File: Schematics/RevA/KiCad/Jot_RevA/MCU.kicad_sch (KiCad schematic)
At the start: 0 parts

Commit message: KiCad MCU: place U1 MDBT50Q-1MV2 module
Co-Authored-By: Claude Opus 5.5 <noreply@anthropic.com>
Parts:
- added U1: MDBT50Q-1MV2, RF_Module:Raytac_MDBT50Q, symbol RF_Module:MDBT50Q-1MV2
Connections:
- new net: U1.1 (GND), U1.15 (GND), U1.2 (GND), U1.33 (GND), U1.55 (GND)
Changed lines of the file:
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@@
 	(generator_version "10.0")
 	(paper "A4")
+	(symbol
+		(lib_id "RF_Module:MDBT50Q-1MV2")
+		(at 142.24 91.44 0)
+		(unit 1)
+		(body_style 1)
+		(exclude_from_sim no)
+		(in_bom yes)
+		(on_board yes)
+		(in_pos_files yes)
+		(dnp no)
+		(fields_autoplaced yes)
+		(property "Reference" "U1"
+			(at 144.3833 137.16 0)
+			(show_name no)
+			(do_not_autoplace no)
+			(effects
+				(font
+					(size 1.27 1.27)
+				)
+				(justify left)
+			)
+		)
+		(property "Value" "MDBT50Q-1MV2"
+			(at 144.3833 139.7 0)
+			(show_name no)
+			(do_not_autoplace no)
+			(effects
+				(font
+					(size 1.27 1.27)
+				)
+				(justify left)
+			)
+		)
+		(property "Footprint" "RF_Module:Raytac_MDBT50Q"
+			(at 142.24 96.52 0)
+			(hide yes)
+			(show_name no)
+			(do_not_autoplace no)
+			(effects
+				(font
+					(size 1.27 1.27)
+				)
+			)
+		)
+		(property "Datasheet" "https://www.raytac.com/download/index.php?index_id=43"
+			(at 142.24 96.52 0)
+			(hide yes)
+			(show_name no)
+			(do_not_autoplace no)
+			(effects
+				(font
+					(size 1.27 1.27)
+				)
+			)
+		)
+		(property "Description" "Multiprotocol BLE/ANT/2.4 GHz/802.15.4 Cortex-M4F SoC, nRF52840 module"
+			(at 142.24 91.44 0)
+			(hide yes)
+			(show_name no)
+			(do_not_autoplace no)
+			(effects
+				(font
+					(size 1.27 1.27)
+				)
+			)
+		)
+		(pin "46"
+		)
+		(pin "37"
+		)
+		(pin "36"
+		)
+		(pin "10"
+		)
+		(pin "11"
+		)
+		(pin "12"
+		)
+		(pin "47"
+		)
+		(pin "48"
+		)
+		(pin "56"
+		)
+		(pin "57"
+		)
+		(pin "61"
+		)
+		(pin "58"
+		)
+		(pin "59"
+		)
+		(pin "60"
+		)
+		(pin "31"
+		)
+		(pin "32"
+		)
+		(pin "28"
+		)
+		(pin "34"
+		)
+		(pin "35"
+		)
+		(pin "29"
+		)
+		(pin "30"
+		)
+		(pin "33"
+		)
+		(pin "6"
+		)
+		(pin "5"
+		)
+		(pin "8"
+		)
+		(pin "7"
+		)
+		(pin "9"
+		)
+		(pin "4"
+		)
+		(pin "3"
+		)
+		(pin "2"
+		)
+		(pin "1"
+		)
+		(pin "49"
+		)
+		(pin "17"
+		)
+		(pin "18"
+		)
+		(pin "13"
+		)
+		(pin "14"
+		)
+		(pin "15"
+		)
+		(pin "16"
+		)
+		(pin "19"
+		)
+		(pin "27"
+		)
+		(pin "20"
+		)
+		(pin "26"
+		)
+		(pin "25"
+		)
+		(pin "21"
+		)
+		(pin "22"
+		)
+		(pin "23"
+		)
+		(pin "24"
+		)
+		(pin "44"
+		)
+		(pin "45"
+		)
+		(pin "42"
+		)
+		(pin "43"
+		)
+		(pin "41"
+		)
+		(pin "40"
+		)
+		(pin "39"
+		)
+		(pin "38"
+		)
+		(pin "55"
+		)
+		(pin "54"
+		)
+		(pin "53"
+		)
+		(pin "52"
+		)
+		(pin "51"
+		)
+		(pin "50"
+		)
+		(instances
+			(project "Jot_RevA"
+				(path "/61747270-9f90-47b6-9c50-5ea1f41f259a/12d7af8c-4dae-4738-915d-dcd3faf7f757"
+					(reference "U1")
+					(unit 1)
+				)
+			)
+		)
+	)
 )

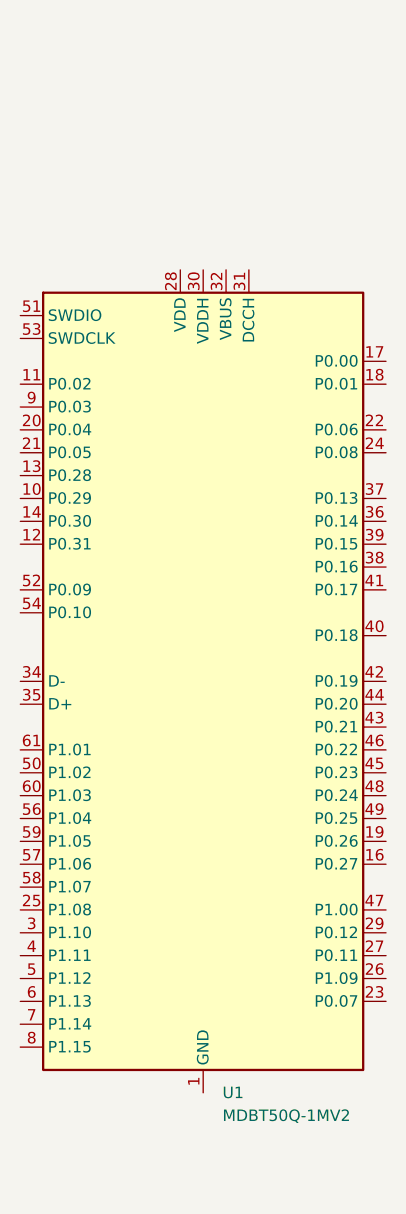
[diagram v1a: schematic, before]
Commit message: KiCad MCU: U1 VDD/VDDH on +3V3 with 10uF, grounds
Co-Authored-By: Claude Opus 5.5 <noreply@anthropic.com>
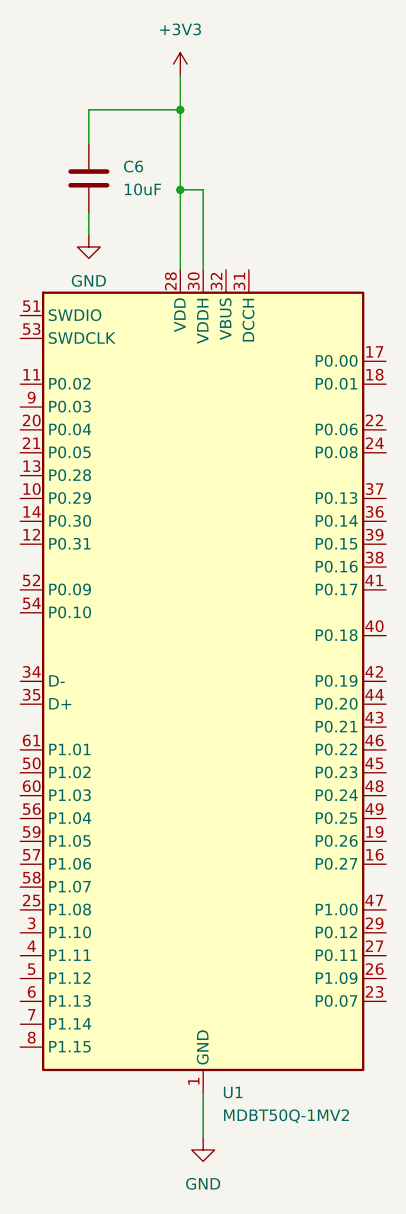
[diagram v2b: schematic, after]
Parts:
- added C6: 10uF, Package_SO:SOIC-8_3.9x4.9mm_P1.27mm, symbol Device:C
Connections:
- net GND: now reaches U1.1 (GND), U1.15 (GND), U1.2 (GND), U1.33 (GND), U1.55 (GND)
- net GND: now also C6.2
- net +3V3: now reaches U1.28 (VDD)
- net +3V3: now also U1.30 (VDDH), C6.1

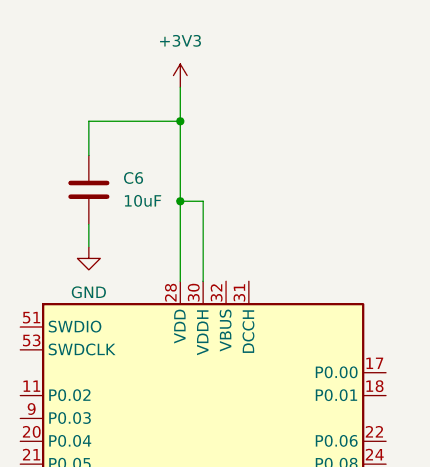
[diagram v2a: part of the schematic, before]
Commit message: KiCad MCU: VBUS via R14 2.2R with 10uF, PWR_FLAG, DCCH no-connect
Co-Authored-By: Claude Opus 5.5 <noreply@anthropic.com>
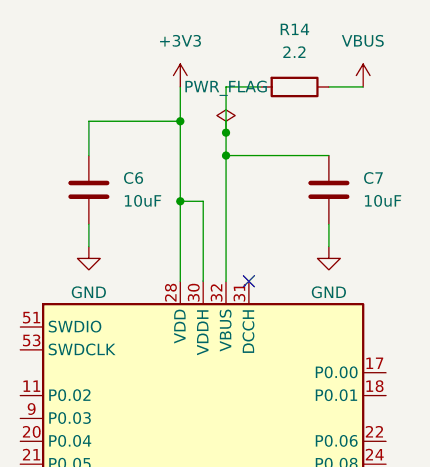
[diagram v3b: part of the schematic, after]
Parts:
- added C7: 10uF, Package_SO:SOIC-8_3.9x4.9mm_P1.27mm, symbol Device:C
- added R14: 2.2, symbol Device:R
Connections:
- net GND: now also C7.2
- net at U1.32 (VBUS): now also C7.1, R14.2
- new net VBUS: R14.1
- no-connect marks 0 -> 1

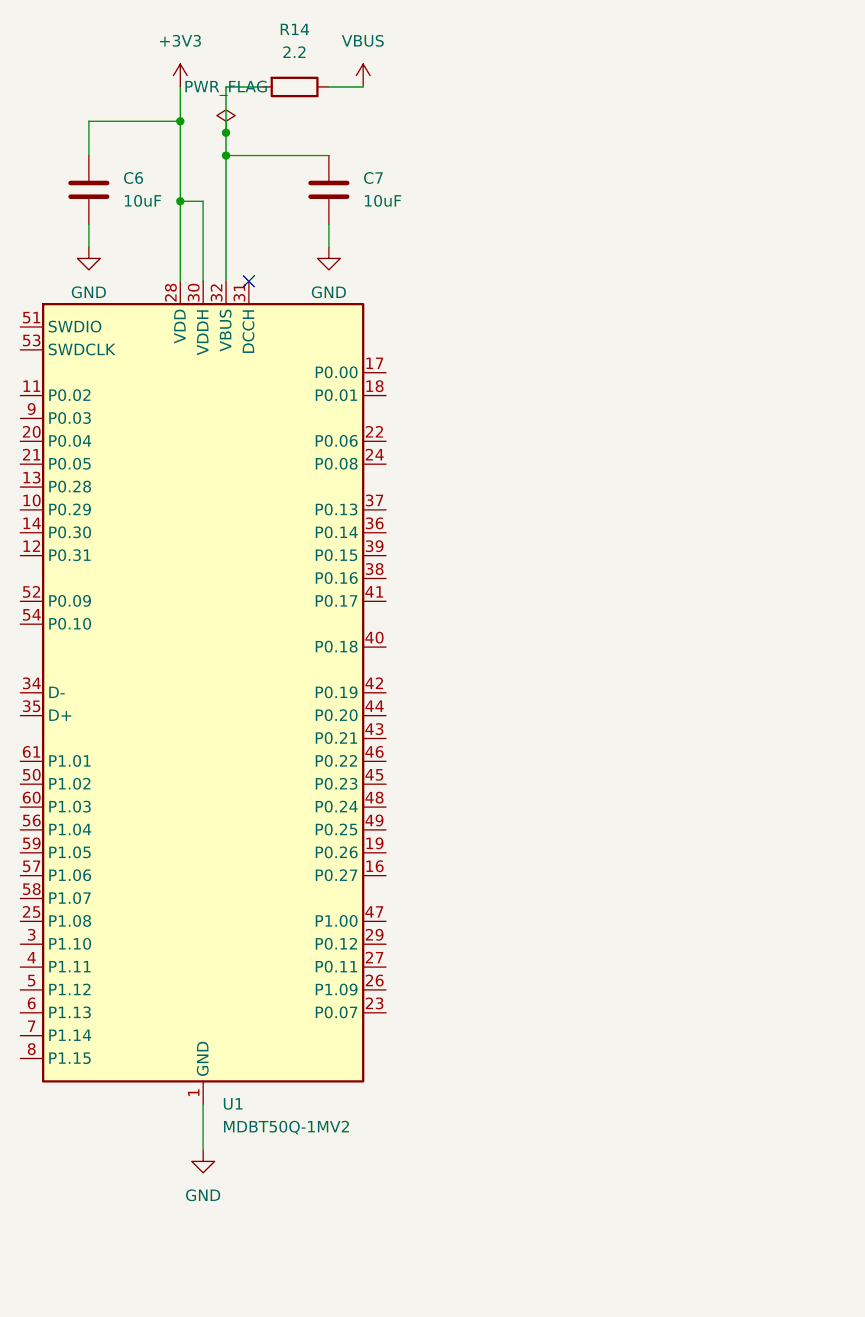
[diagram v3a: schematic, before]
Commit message: KiCad: tidy MCU power cluster and spacing; fill MCU/Power title blocks
Co-Authored-By: Claude Opus 5.5 <noreply@anthropic.com>
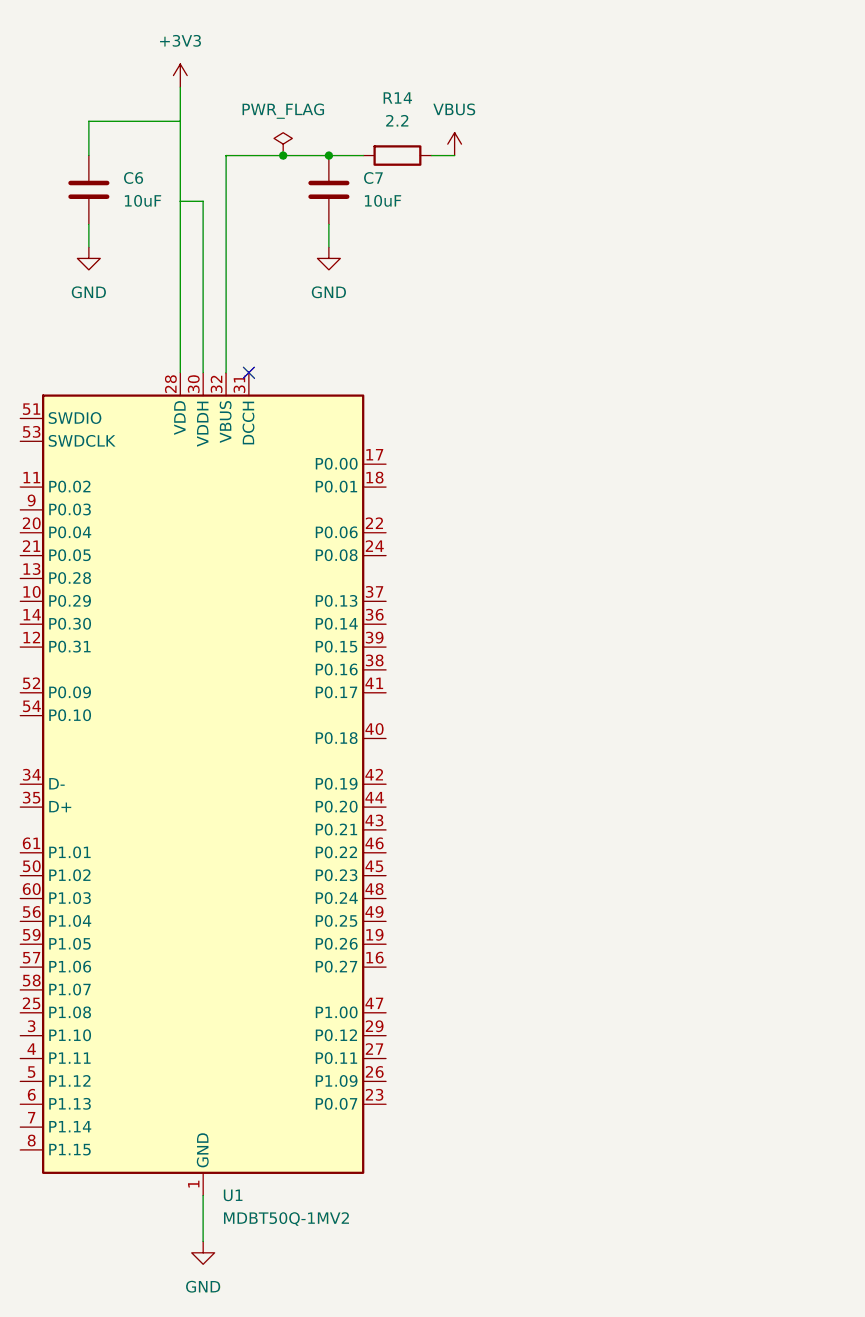
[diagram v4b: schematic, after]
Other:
- company: (none) -> James Donal Cronin
- title: (none) -> Jot Rev A: MCU
- moved on the sheet: R14, U1
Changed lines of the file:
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@@
 	(generator_version "10.0")
 	(paper "A4")
+	(title_block
+		(title "Jot Rev A: MCU")
+		(date "2026-10-02")
+		(rev "A")
+		(company "James Donal Cronin")
+		(comment 1 "JOT-HW-001: handheld push-to-talk voice capture")
+	)
+	(no_connect
+		(at 147.32 55.88)
+	)
+	(wire
+		(pts
+			(xy 144.78 31.75) (xy 151.13 31.75)
+		)
+		(stroke
+			(width 0)
+			(type default)
+		)
+	)
+	(wire
+		(pts
+			(xy 151.13 31.75) (xy 156.21 31.75)
+		)
+		(stroke
+			(width 0)
+			(type default)
+		)
+	)
+	(wire
+		(pts
+			(xy 156.21 31.75) (xy 160.02 31.75)
+		)
+		(stroke
+			(width 0)
+			(type default)
+		)
+	)
+	(wire
+		(pts
+			(xy 167.64 31.75) (xy 170.18 31.75)
+		)
+		(stroke
+			(width 0)
+			(type default)
+		)
+	)
 	(junction
-		(at 139.7 27.94)
+		(at 151.13 31.75)
 		(diameter 0)
 		(color 0 0 0 0)
 	)
 	(junction
-		(at 144.78 29.21)
+		(at 156.21 31.75)
 		(diameter 0)
 		(color 0 0 0 0)
 	)
-	(junction
-		(at 139.7 36.83)
-		(diameter 0)
-		(color 0 0 0 0)
-	)
-	(junction
-		(at 144.78 31.75)
-		(diameter 0)
-		(color 0 0 0 0)
-	)
-	(no_connect
-		(at 147.32 45.72)
-	)
 	(wire
 		(pts
@@
 	(wire
 		(pts
-			(xy 139.7 36.83) (xy 139.7 45.72)
-		)
-		(stroke
-			(width 0)
-			(type default)
-		)
-	)
-	(wire
-		(pts
-			(xy 144.78 29.21) (xy 144.78 24.13)
-		)
-		(stroke
-			(width 0)
-			(type default)
-		)
-	)
-	(wire
-		(pts
-			(xy 144.78 45.72) (xy 144.78 31.75)
-		)
-		(stroke
-			(width 0)
-			(type default)
-		)
-	)
-	(wire
-		(pts
-			(xy 142.24 45.72) (xy 142.24 36.83)
+			(xy 139.7 36.83) (xy 139.7 55.88)
+		)
+		(stroke
+			(width 0)
+			(type default)
+		)
+	)
+	(wire
+		(pts
+			(xy 144.78 55.88) (xy 144.78 31.75)
+		)
+		(stroke
+			(width 0)
+			(type default)
+		)
+	)
+	(wire
+		(pts
+			(xy 142.24 55.88) (xy 142.24 36.83)
 		)
 		(stroke
@@
 	(wire
 		(pts
-			(xy 144.78 31.75) (xy 156.21 31.75)
-		)
-		(stroke
-			(width 0)
-			(type default)
-		)
-	)
-	(wire
-		(pts
-			(xy 144.78 31.75) (xy 144.78 29.21)
-		)
-		(stroke
-			(width 0)
-			(type default)
-		)
-	)
-	(wire
-		(pts
 			(xy 139.7 27.94) (xy 139.7 36.83)
 		)
@@
 	(wire
 		(pts
-			(xy 142.24 137.16) (xy 142.24 142.24)
-		)
-		(stroke
-			(width 0)
-			(type default)
-		)
-	)
-	(wire
-		(pts
-			(xy 156.21 24.13) (xy 160.02 24.13)
-		)
-		(stroke
-			(width 0)
-			(type default)
-		)
-	)
-	(wire
-		(pts
-			(xy 144.78 24.13) (xy 148.59 24.13)
+			(xy 142.24 147.32) (xy 142.24 152.4)
 		)
 		(stroke
@@
 	(symbol
 		(lib_id "power:PWR_FLAG")
-		(at 144.78 29.21 0)
+		(at 151.13 31.75 0)
 		(unit 1)
 		(body_style 1)
@@
 		(fields_autoplaced yes)
 		(property "Reference" "#FLG03"
-			(at 144.78 27.305 0)
+			(at 151.13 29.845 0)
 			(hide yes)
 			(show_name no)
@@
 		)
 		(property "Value" "PWR_FLAG"
-			(at 144.78 24.13 0)
+			(at 151.13 26.67 0)
 			(show_name no)
 			(do_not_autoplace no)
@@
 		)
 		(property "Footprint" ""
-			(at 144.78 29.21 0)
+			(at 151.13 31.75 0)
 			(hide yes)
 			(show_name no)
@@
 		)
 		(property "Datasheet" ""
-			(at 144.78 29.21 0)
+			(at 151.13 31.75 0)
 			(hide yes)
 			(show_name no)
@@
 		)
 		(property "Description" "Special symbol for telling ERC where power comes from"
-			(at 144.78 29.21 0)
+			(at 151.13 31.75 0)
 			(hide yes)
 			(show_name no)
@@
 	(symbol
 		(lib_id "power:GND")
-		(at 142.24 142.24 0)
+		(at 142.24 152.4 0)
 		(unit 1)
 		(body_style 1)
@@
 		(fields_autoplaced yes)
 		(property "Reference" "#PWR01"
-			(at 142.24 148.59 0)
+			(at 142.24 158.75 0)
 			(hide yes)
 			(show_name no)
@@
 		)
 		(property "Value" "GND"
-			(at 142.24 147.32 0)
+			(at 142.24 157.48 0)
 			(show_name no)
 			(do_not_autoplace no)
@@
 		)
 		(property "Footprint" ""
-			(at 142.24 142.24 0)
+			(at 142.24 152.4 0)
 			(hide yes)
 			(show_name no)
@@
 		)
 		(property "Datasheet" ""
-			(at 142.24 142.24 0)
+			(at 142.24 152.4 0)
 			(hide yes)
 			(show_name no)
@@
 		)
 		(property "Description" "Power symbol creates a global label with name \"GND\" , ground"
-			(at 142.24 142.24 0)
+			(at 142.24 152.4 0)
 			(hide yes)
 			(show_name no)
@@
 	(symbol
 		(lib_id "RF_Module:MDBT50Q-1MV2")
-		(at 142.24 91.44 0)
+		(at 142.24 101.6 0)
 		(unit 1)
 		(body_style 1)
@@
 		(fields_autoplaced yes)
 		(property "Reference" "U1"
-			(at 144.3833 137.16 0)
+			(at 144.3833 147.32 0)
 			(show_name no)
 			(do_not_autoplace no)
@@
 		)
 		(property "Value" "MDBT50Q-1MV2"
-			(at 144.3833 139.7 0)
+			(at 144.3833 149.86 0)
 			(show_name no)
 			(do_not_autoplace no)
@@
 		)
 		(property "Footprint" "RF_Module:Raytac_MDBT50Q"
-			(at 142.24 96.52 0)
+			(at 142.24 106.68 0)
 			(hide yes)
 			(show_name no)
@@
 		)
 		(property "Datasheet" "https://www.raytac.com/download/index.php?index_id=43"
-			(at 142.24 96.52 0)
+			(at 142.24 106.68 0)
 			(hide yes)
 			(show_name no)
@@
 		)
 		(property "Description" "Multiprotocol BLE/ANT/2.4 GHz/802.15.4 Cortex-M4F SoC, nRF52840 module"
-			(at 142.24 91.44 0)
+			(at 142.24 101.6 0)
 			(hide yes)
 			(show_name no)
@@
 	(symbol
 		(lib_id "power:VBUS")
-		(at 160.02 24.13 0)
+		(at 170.18 31.75 0)
 		(unit 1)
 		(body_style 1)
@@
 		(fields_autoplaced yes)
 		(property "Reference" "#PWR027"
-			(at 160.02 27.94 0)
+			(at 170.18 35.56 0)
 			(hide yes)
 			(show_name no)
@@
 		)
 		(property "Value" "VBUS"
-			(at 160.02 19.05 0)
+			(at 170.18 26.67 0)
 			(show_name no)
 			(do_not_autoplace no)
@@
 		)
 		(property "Footprint" ""
-			(at 160.02 24.13 0)
+			(at 170.18 31.75 0)
 			(hide yes)
 			(show_name no)
@@
 		)
 		(property "Datasheet" ""
-			(at 160.02 24.13 0)
+			(at 170.18 31.75 0)
 			(hide yes)
 			(show_name no)
@@
 		)
 		(property "Description" "Power symbol creates a global label with name \"VBUS\""
-			(at 160.02 24.13 0)
+			(at 170.18 31.75 0)
 			(hide yes)
 			(show_name no)
@@
 	(symbol
 		(lib_id "Device:R")
-		(at 152.4 24.13 270)
+		(at 163.83 31.75 270)
 		(unit 1)
 		(body_style 1)
@@
 		(fields_autoplaced yes)
 		(property "Reference" "R14"
-			(at 152.4 17.78 90)
+			(at 163.83 25.4 90)
 			(show_name no)
 			(do_not_autoplace no)
@@
 		)
 		(property "Value" "2.2"
-			(at 152.4 20.32 90)
+			(at 163.83 27.94 90)
 			(show_name no)
 			(do_not_autoplace no)
@@
 		)
 		(property "Footprint" ""
-			(at 152.4 22.352 90)
+			(at 163.83 29.972 90)
 			(hide yes)
 			(show_name no)
@@
 		)
 		(property "Datasheet" ""
-			(at 152.4 24.13 0)
+			(at 163.83 31.75 0)
 			(hide yes)
 			(show_name no)
@@
 		)
 		(property "Description" "Resistor"
-			(at 152.4 24.13 0)
-			(hide yes)
-			(show_name no)
+			(at 163.83 31.75 0)
+			(hide yes)
+			(show_name no)

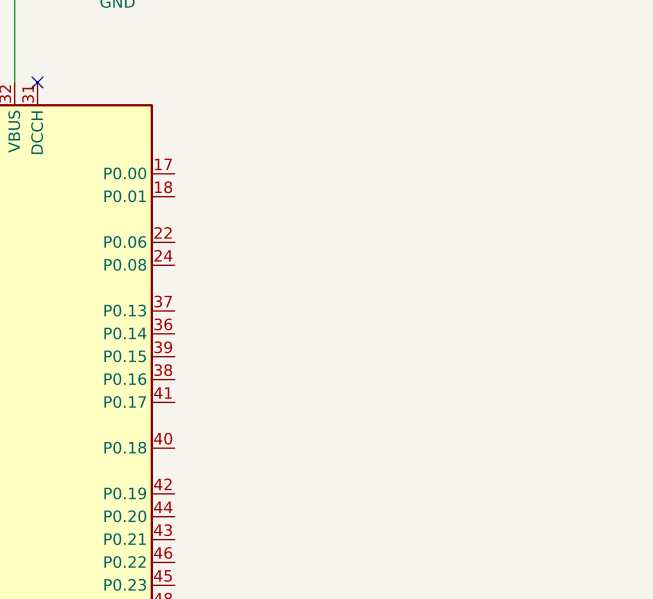
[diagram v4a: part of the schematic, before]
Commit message: MCU sheet: 32.768 kHz crystal Y1 on P0.00/P0.01 with 18 pF caps
Co-Authored-By: Claude Opus 5.5 <noreply@anthropic.com>
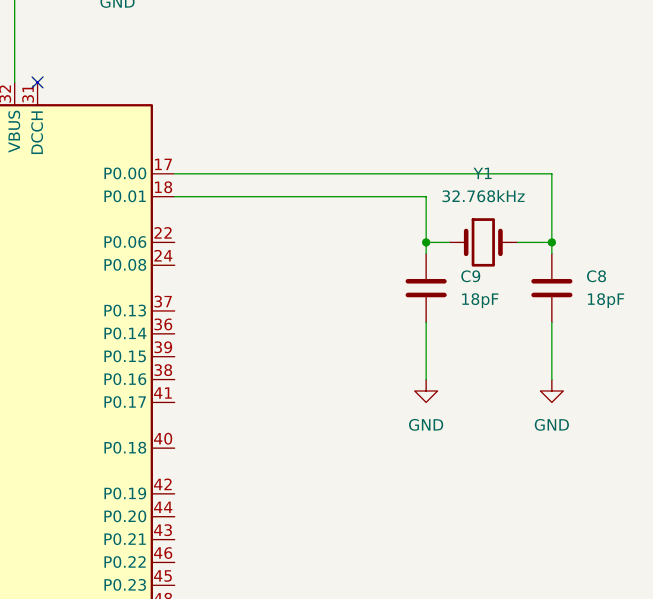
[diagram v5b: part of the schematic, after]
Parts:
- added C8, C9: 18pF, symbol Device:C
- added Y1: 32.768kHz, Relay_THT:Relay_SPDT_HsinDa_Y14, symbol Device:Crystal
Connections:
- net GND: now also C8.2, C9.2
- net at U1.17 (P0.00): now also C8.1, Y1.2
- net at U1.18 (P0.01): now also C9.1, Y1.1
